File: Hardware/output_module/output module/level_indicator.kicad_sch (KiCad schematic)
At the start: 42 parts, among them U2 TL074

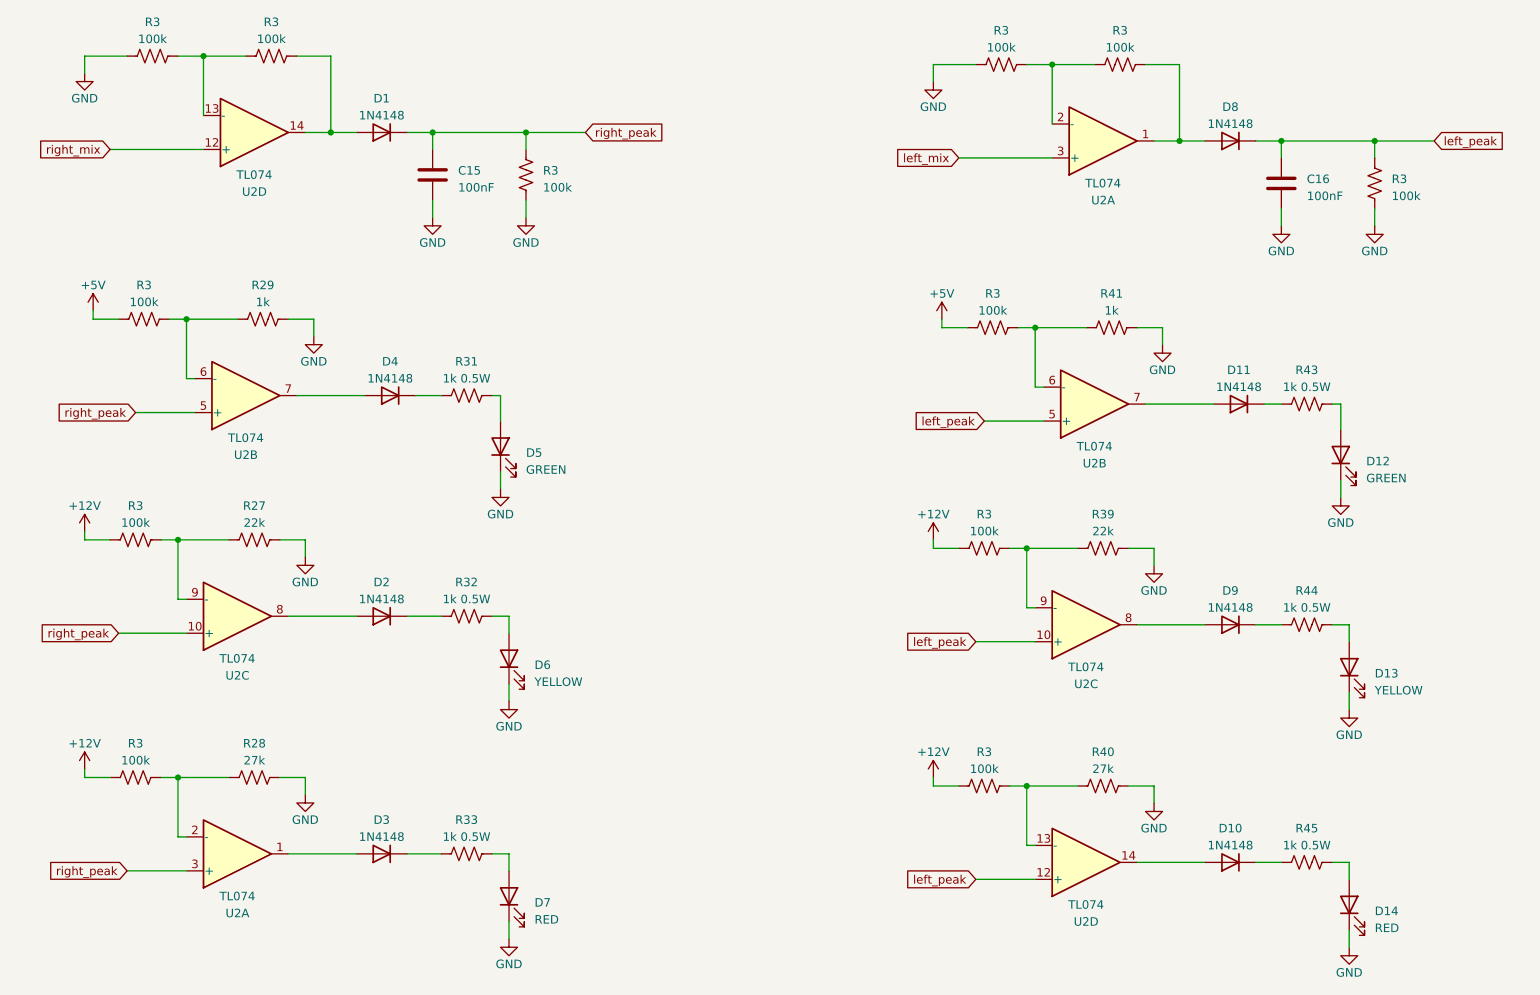
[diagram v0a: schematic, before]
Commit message: proto order
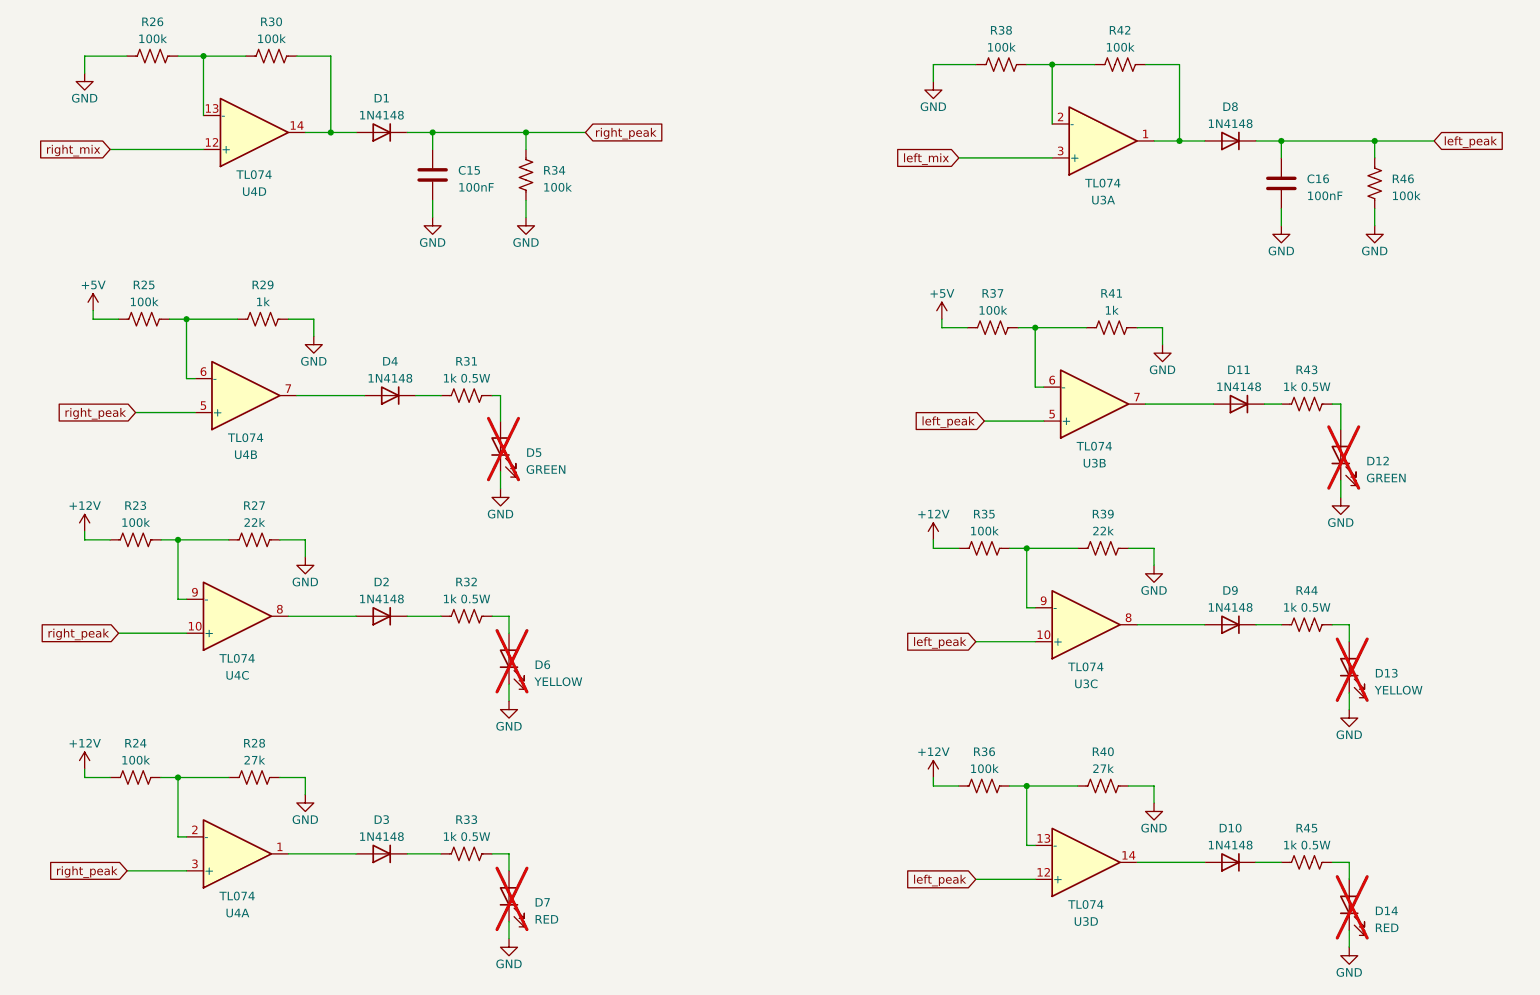
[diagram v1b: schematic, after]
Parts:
- D12, D13, D14, D5, D6, D7: now not fitted
- renumbered R3 to R23, R3 to R24, R3 to R25, R3 to R26, R3 to R30, R3 to R34, R3 to R35, R3 to R36, R3 to R37, R3 to R38, R3 to R42, R3 to R46, U2 to U3, U2 to U4

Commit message: update output module production mistakes
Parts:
- D12, D13, D14, D5, D6, D7: now fitted
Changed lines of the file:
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@@
 		(in_bom yes)
 		(on_board yes)
-		(dnp yes)
+		(dnp no)
 		(fields_autoplaced yes)
 		(property "Reference" "D7"
@@
 		(in_bom yes)
 		(on_board yes)
-		(dnp yes)
+		(dnp no)
 		(fields_autoplaced yes)
 		(property "Reference" "D13"
@@
 		(in_bom yes)
 		(on_board yes)
-		(dnp yes)
+		(dnp no)
 		(fields_autoplaced yes)
 		(property "Reference" "D12"
@@
 		(in_bom yes)
 		(on_board yes)
-		(dnp yes)
+		(dnp no)
 		(fields_autoplaced yes)
 		(property "Reference" "D6"
@@
 		(in_bom yes)
 		(on_board yes)
-		(dnp yes)
+		(dnp no)
 		(fields_autoplaced yes)
 		(property "Reference" "D5"
@@
 		(in_bom yes)
 		(on_board yes)
-		(dnp yes)
+		(dnp no)
 		(fields_autoplaced yes)
 		(property "Reference" "D14"
